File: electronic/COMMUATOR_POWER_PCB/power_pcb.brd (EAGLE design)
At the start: 100 x 30.5 mm, 9 parts, among them IC1 L293D, K1 CB1A-P-12V, K2 CB1A-P-12V

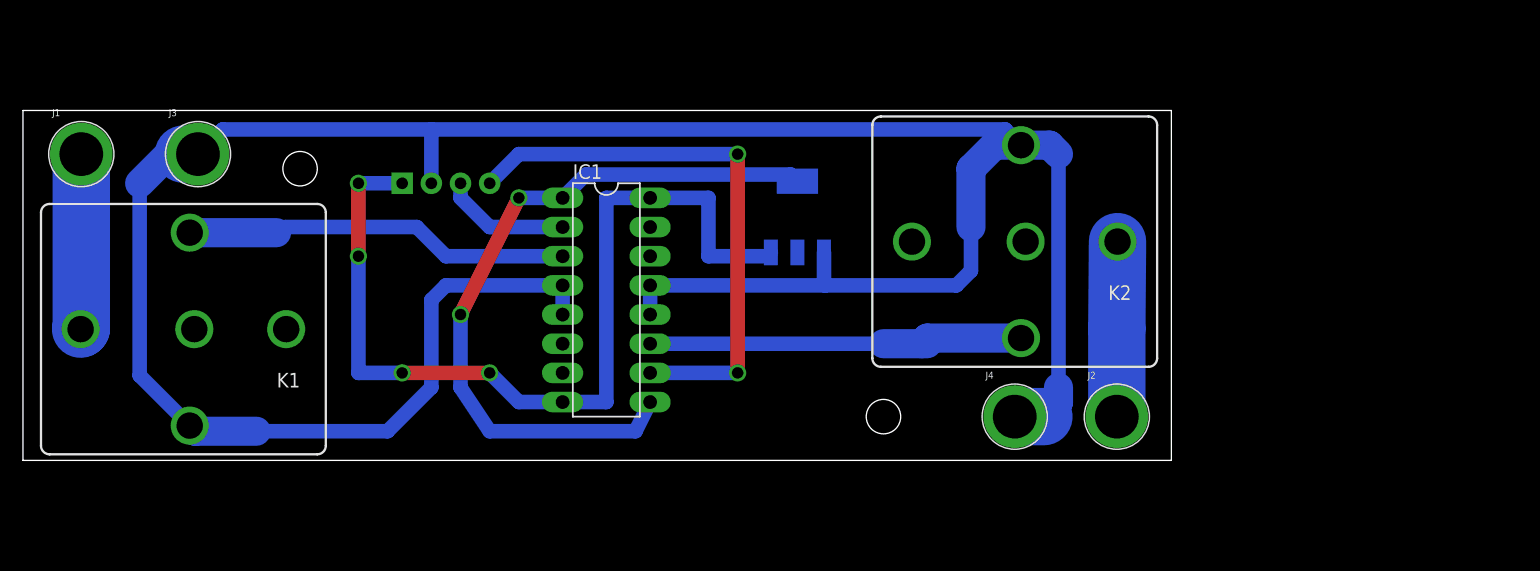
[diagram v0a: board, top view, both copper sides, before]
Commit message: add power commutator
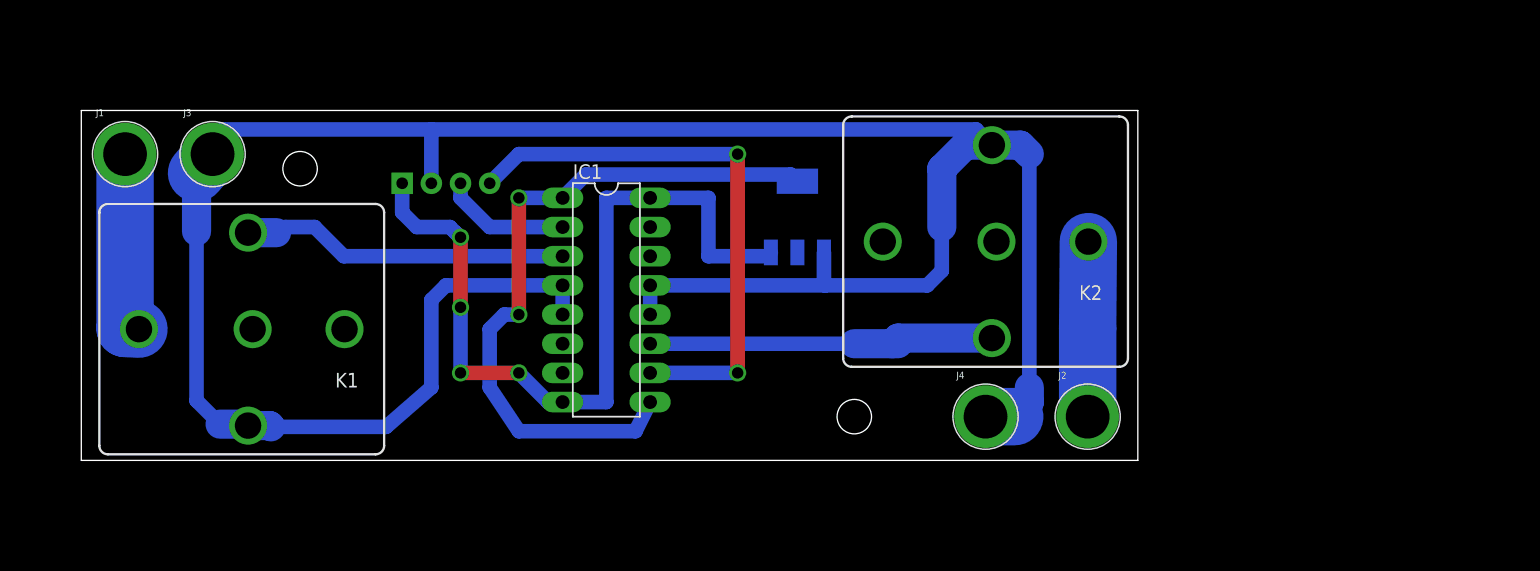
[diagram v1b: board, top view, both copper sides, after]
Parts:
- moved K1 5.08 mm to (19.1, 11.4)
- moved J1 3.81 mm to (8.89, 26.7)
- moved J2 2.54 mm to (92.7, 3.81)
- moved J4 2.54 mm to (83.8, 3.81)
- moved K2 2.54 mm to (83.8, 19.1)
- moved J3 1.27 mm to (16.5, 26.7)
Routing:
- net GND: track 230.6 -> 217.7 mm
- net +12V: track 80.3 -> 71.4 mm
- net REL1: track 33.8 -> 28.8 mm
- net REL2: track 36.3 -> 33.8 mm
- net +3V3: track 63.2 -> 61.2 mm
- net N$1: track 15.3 -> 16.4 mm
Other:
- board size 100 x 30.5 mm -> 92 x 30.5 mm

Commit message: change power pcb
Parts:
- removed IC1: L293D, st-microelectronics:DIL16
- removed K1: CB1A-P-12V, relay:CB1
- removed U1: (no value), SparkFun-IC-Power:SOT223
- added D1: 1N4004, diode:DO41-10
- added J6: (no value), SparkFun-Connectors:SCREWTERMINAL-5MM-2
- added U$2: 12v, diy-modules:DC-DC-STEP-DOWN-MP1584
- added U$3: usb2, diy-modules:DC-DC-STEP-DOWN-MP1584
- added U$4: USb1, diy-modules:DC-DC-STEP-DOWN-MP1584
- added U$5: Jet2, diy-modules:DC-DC-STEP-DOWN-MP1584
- added U$6: Jet1, diy-modules:DC-DC-STEP-DOWN-MP1584
- added U2: (no value), SparkFun-IC-Power:TO220-IGO
- J1, J3: device SparkFun-Connectors:BANANA_CONN -> SparkFun-Connectors:SCREWTERMINAL-5MM-2
- J5: device SparkFun-Connectors:MOLEX-1X4 -> SparkFun-Connectors:SCREWTERMINAL-5MM-2
- moved J1 74.0 mm to (82.5, 34.3), turned to 180 degrees
- moved J2 43.3 mm to (125.7, 31.8)
- moved J4 43.3 mm to (116.8, 31.8)
- moved K2 33.2 mm to (116.8, 15.2)
- moved J5 19.4 mm to (49.5, 34.3)
- moved J3 15.9 mm to (30.5, 34.3), turned to 180 degrees
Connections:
- removed net +12V: IC1.16, IC1.8, J5.1, U1.3
- removed net +3V3: IC1.1, IC1.9, U1.2, U1.4
- removed net N$1: J1.P$1, K1.30
- removed net REL1: IC1.3, K1.85
- removed net REL2: IC1.11, K2.86
- removed net RELIN1: IC1.2, J5.3
- removed net RELIN2: IC1.10, J5.4
- new net N$11: D1.C, K2.86, U2.OUT
- new net N$13: J6.2, U2.IN
- new net N$4: J1.1, U$5.OUT+.1, U$5.OUT+.2, U$6.OUT+.1, U$6.OUT+.2
- new net N$5: J1.2, U$5.OUT-.1, U$5.OUT-.2, U$6.OUT-.1, U$6.OUT-.2
- new net N$6: J3.2, U$3.OUT-.1, U$3.OUT-.2, U$4.OUT-.1, U$4.OUT-.2
- new net N$7: J3.1, U$3.OUT+.1, U$3.OUT+.2, U$4.OUT+.1, U$4.OUT+.2
- new net N$8: J5.1, U$2.OUT-.1, U$2.OUT-.2
- new net N$9: J5.2, U$2.OUT+.1, U$2.OUT+.2
- net GND: now also D1.A, U$2.IN-.1, U$2.IN-.2, U$3.IN-.1, U$3.IN-.2, U$4.IN-.1, U$4.IN-.2, U$5.IN-.1, U$5.IN-.2, U$6.IN-.1, U$6.IN-.2, U2.GND; no longer IC1.12, IC1.13, IC1.4, IC1.5, J3.P$1, J5.2, K1.86, U1.1
- net N$2: now also J6.1
- net V+: now also U$2.IN+.1, U$2.IN+.2, U$3.IN+.1, U$3.IN+.2, U$4.IN+.1, U$4.IN+.2, U$5.IN+.1, U$5.IN+.2, U$6.IN+.1, U$6.IN+.2; no longer K1.87
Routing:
- net V+: track 0.00 -> 143.9 mm
- net +12V: track 71.4 -> 0.00 mm, vias 4 -> 0
- net +3V3: track 61.2 -> 0.00 mm, vias 2 -> 0
- net N$4: track 0.00 -> 49.4 mm
- net RELIN2: track 49.3 -> 0.00 mm, vias 2 -> 0
- net N$7: track 0.00 -> 47.8 mm
- net REL2: track 33.8 -> 0.00 mm
- net N$6: track 0.00 -> 29.6 mm
- net N$5: track 0.00 -> 29.6 mm
- net REL1: track 28.8 -> 0.00 mm
- net N$11: track 0.00 -> 22.8 mm
- net N$2: track 15.2 -> 36.0 mm
- net N$1: track 16.4 -> 0.00 mm
- net GND: track 217.7 -> 230.7 mm
- net N$9: track 0.00 -> 12.7 mm
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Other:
- board size 92 x 30.5 mm -> 125 x 45.7 mm

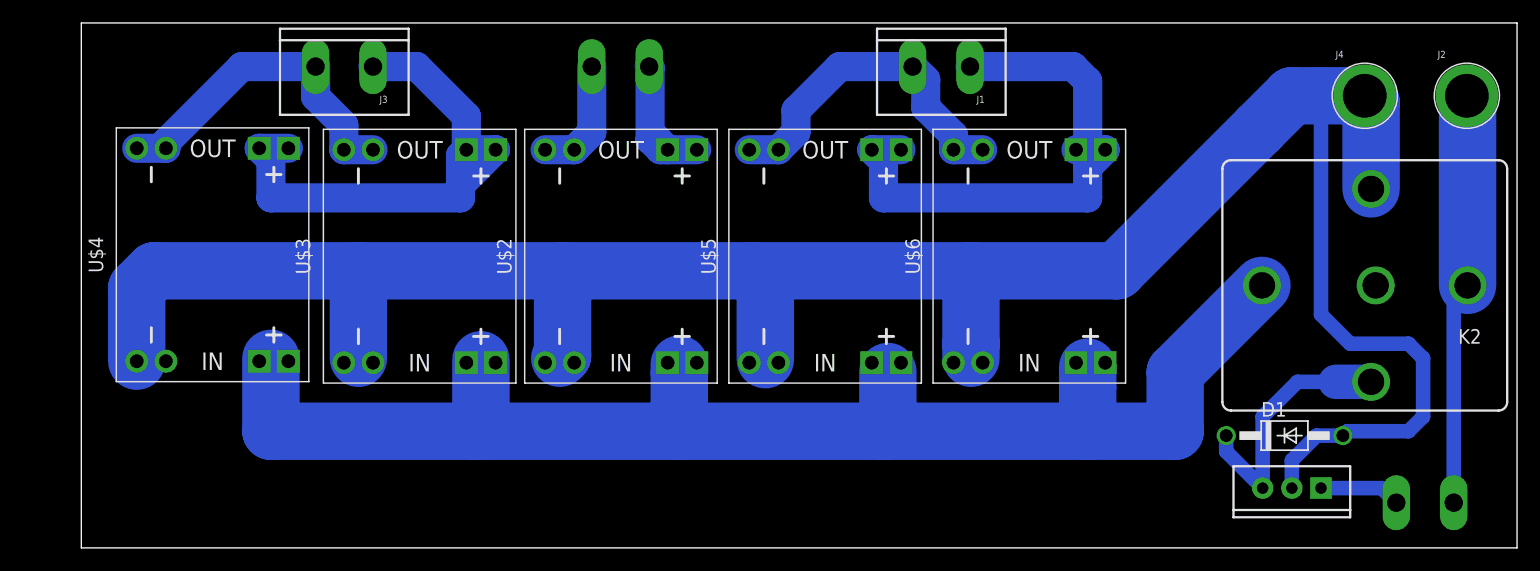
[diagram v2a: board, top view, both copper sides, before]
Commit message: change outside walls
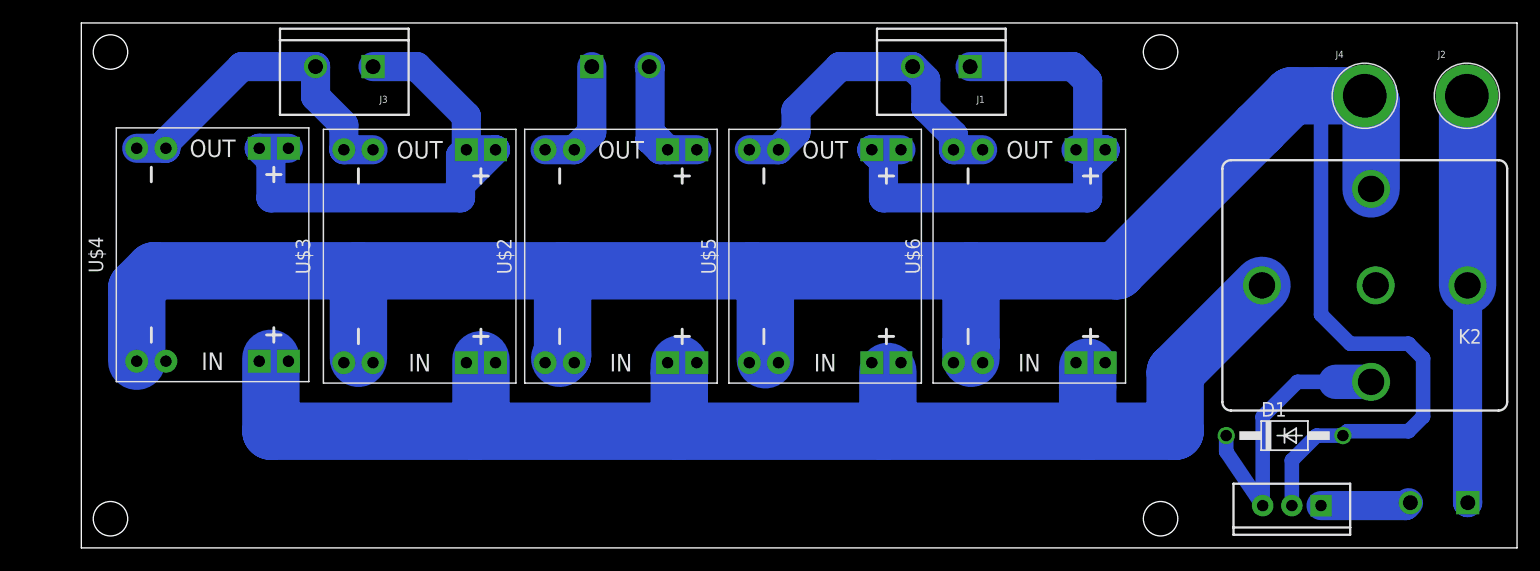
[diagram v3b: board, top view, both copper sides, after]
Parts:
- moved U2 1.52 mm to (110.5, -3.94)
- moved J6 1.22 mm to (125.8, -3.68)
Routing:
- net N$11: track 22.8 -> 25.5 mm
- net GND: track 230.7 -> 232.2 mm
- net N$13: track 7.08 -> 7.89 mm
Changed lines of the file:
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@@
 <wire x1="130.099" y1="38.09" x2="5.08" y2="38.09" width="0" layer="20"/>
 <wire x1="5.08" y1="38.09" x2="5.08" y2="-7.62" width="0" layer="20"/>
+<hole x="7.62" y="35.56" drill="3"/>
+<hole x="7.62" y="-5.08" drill="3"/>
+<hole x="99.06" y="-5.08" drill="3"/>
+<hole x="99.06" y="35.56" drill="3"/>
 </plain>
 <attributes>
@@
 <attribute name="SF_SKU" value="PRT-08432" x="49.53" y="34.29" size="1.778" layer="28" rot="MR180" display="off"/>
 </element>
-<element name="U2" library="SparkFun-IC-Power" package="TO220-IGO" value="" x="110.49" y="-2.413" rot="R180"/>
-<element name="J6" library="SparkFun-Connectors" package="SCREWTERMINAL-5MM-2" value="" x="124.587" y="-3.683" rot="MR0">
-<attribute name="SF_SKU" value="PRT-08432" x="124.587" y="-3.683" size="1.778" layer="28" rot="MR0" display="off"/>
+<element name="U2" library="SparkFun-IC-Power" package="TO220-IGO" value="" x="110.49" y="-3.937" rot="R180"/>
+<element name="J6" library="SparkFun-Connectors" package="SCREWTERMINAL-5MM-2" value="" x="125.81" y="-3.683" rot="MR0">
+<attribute name="SF_SKU" value="PRT-08432" x="125.81" y="-3.683" size="1.778" layer="28" rot="MR0" display="off"/>
 </element>
 </elements>
@@
 <contactref element="D1" pad="A"/>
 <wire x1="107.6325" y1="28.8925" x2="95.25" y2="16.51" width="5" layer="16"/>
-<wire x1="110.49" y1="-2.413" x2="110.49" y2="0" width="1.27" layer="16"/>
+<wire x1="110.49" y1="-3.937" x2="110.49" y2="0" width="1.27" layer="16"/>
 <wire x1="112.649" y1="2.159" x2="114.935" y2="2.159" width="1.27" layer="16"/>
 <wire x1="110.49" y1="0" x2="112.649" y2="2.159" width="1.27" layer="16"/>
@@
 <wire x1="125.79" y1="31.69" x2="125.79" y2="15.24" width="5" layer="16"/>
 <contactref element="J6" pad="1"/>
-<wire x1="124.587" y1="-3.683" x2="124.587" y2="14.037" width="1.27" layer="16"/>
-<wire x1="124.587" y1="14.037" x2="125.79" y2="15.24" width="1.27" layer="16"/>
+<wire x1="125.79" y1="15.24" x2="125.79" y2="-3.663" width="2.54" layer="16"/>
+<wire x1="125.79" y1="-3.663" x2="125.81" y2="-3.683" width="2.54" layer="16"/>
 </signal>
 <signal name="N$4">
@@
 <contactref element="U2" pad="OUT"/>
 <wire x1="104.775" y1="2.159" x2="104.775" y2="0.762" width="1.27" layer="16"/>
-<wire x1="104.775" y1="0.762" x2="107.95" y2="-2.413" width="1.27" layer="16"/>
-<wire x1="107.95" y1="-2.413" x2="107.95" y2="3.81" width="1.27" layer="16"/>
+<wire x1="104.775" y1="0.762" x2="107.95" y2="-3.937" width="1.27" layer="16"/>
+<wire x1="107.95" y1="-3.937" x2="107.95" y2="3.81" width="1.27" layer="16"/>
 <wire x1="107.95" y1="3.81" x2="110.98" y2="6.84" width="1.27" layer="16"/>
 <wire x1="114.3" y1="6.84" x2="110.98" y2="6.84" width="1.27" layer="16"/>
@@
 <contactref element="J6" pad="2"/>
 <contactref element="U2" pad="IN"/>
-<wire x1="113.03" y1="-2.413" x2="118.317" y2="-2.413" width="1.27" layer="16"/>
-<wire x1="118.317" y1="-2.413" x2="119.587" y2="-3.683" width="1.27" layer="16"/>
+<wire x1="120.65" y1="-3.683" x2="120.81" y2="-3.683" width="1.27" layer="16"/>
+<wire x1="113.03" y1="-3.937" x2="120.396" y2="-3.937" width="2.54" layer="16"/>
+<wire x1="120.396" y1="-3.937" x2="120.65" y2="-3.683" width="2.54" layer="16"/>
 </signal>
 </signals>
